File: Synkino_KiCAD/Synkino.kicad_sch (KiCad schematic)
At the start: 161 parts, among them J1 Pwr, J10 EYE8_OUT, J11 EYE4_OUT, J12 Eye, J13 EYE5_OUT, J2 Eye, J3 3.5mm, J4 Micro_SD_Card_Det_Hirose_DM3AT, J5 EYE1_OUT, J6 EYE6_OUT, J7 EYE2_OUT, J8 EYE7_OUT, J9 EYE3_OUT, Q1 IRF7319, Q2 BC847 o. SS8050, Q3 IRLML2244 o. AO3401A, SW1 Power, SW2 Rotary_Encoder_Switch, SW3 Reset, U1 ME6210A50PG, U10 ATMEGA328P-AU, U11 QRE1113GR, U12 QRE1113GR, U13 QRE1113GR, U14 QRE1113GR, U15 QRE1113GR, U16 QRE1113GR, U17 24LC256, U18 QRE1113GR, U2 ATMEGA328P-AU, U3 74HC4050, U4 SPIOLED128x64, U5 AP7312-1833W6-7, U6 74HC14, U7 VS1053B, U8 GS3005, U9 QRE1113GR, X1 FTDIconn, X2 ICSP, X3 FTDIconn, X4 ICSP, Y1 16Mhz, Y2 12.288MHz, Y3 16Mhz

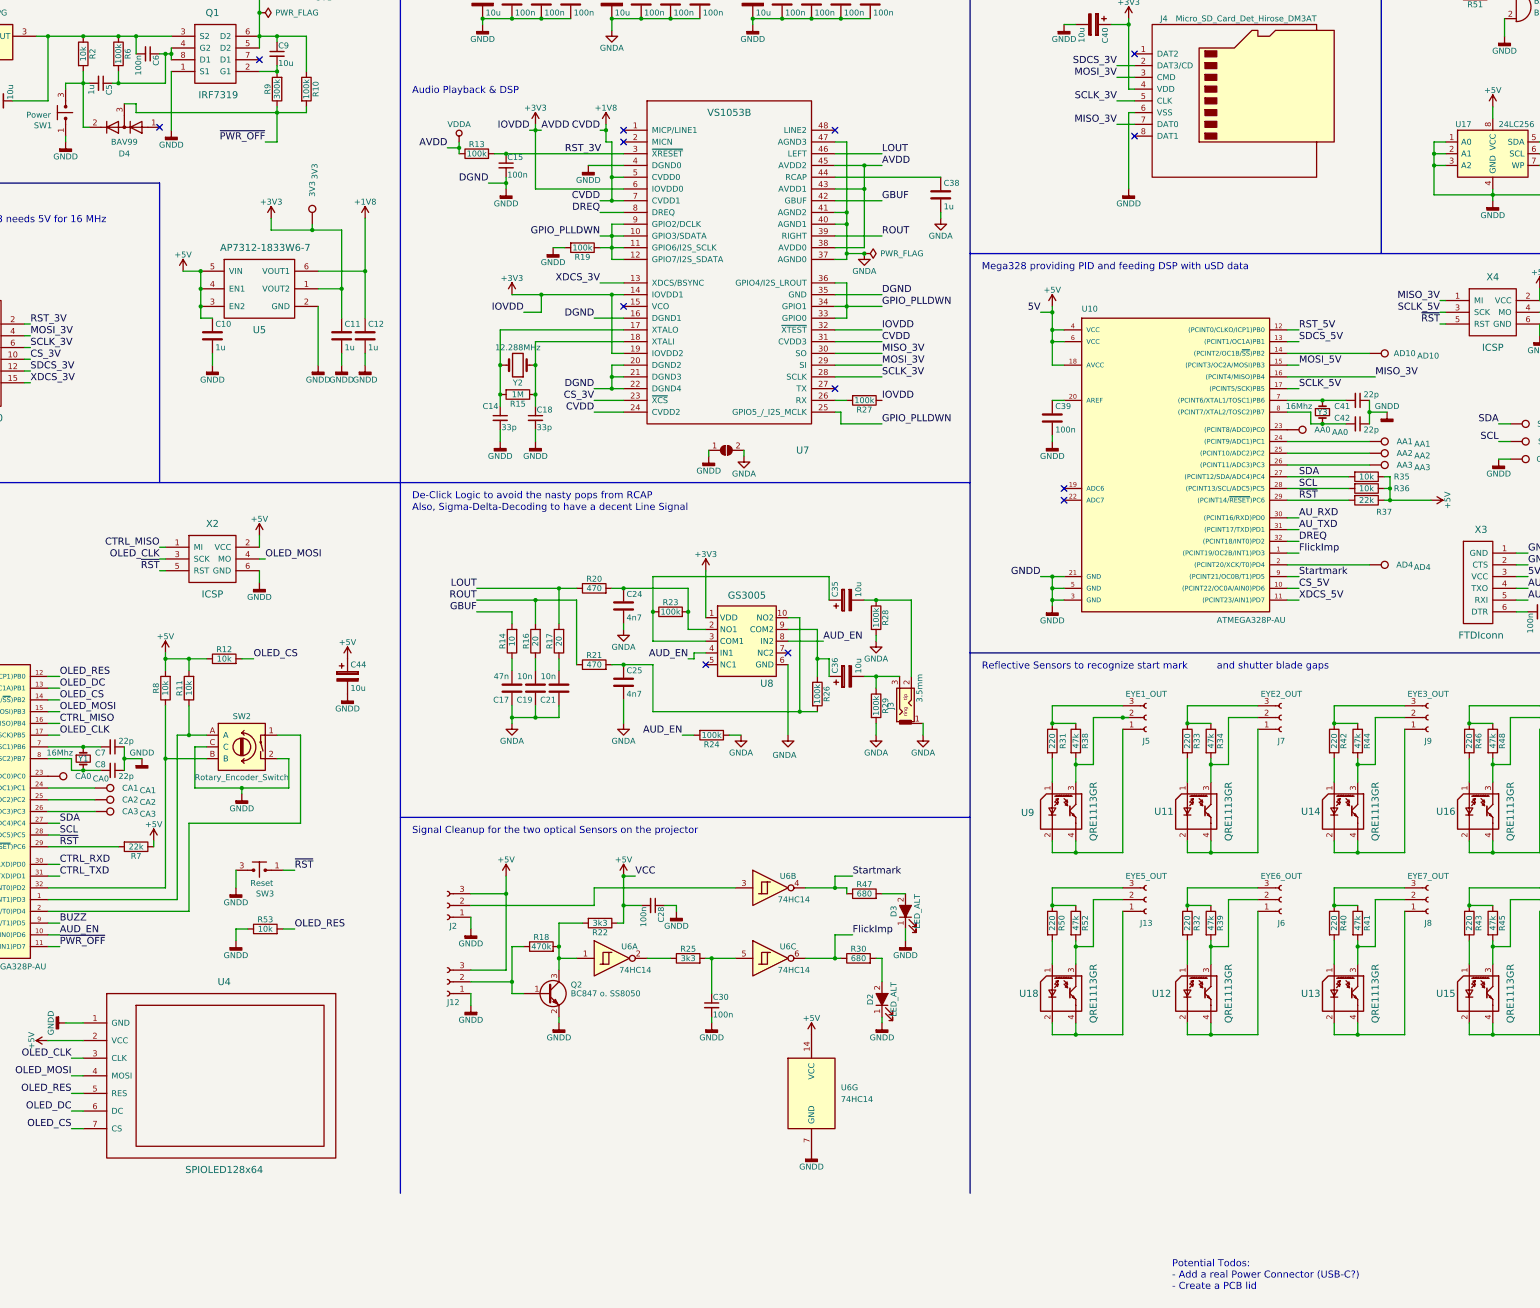
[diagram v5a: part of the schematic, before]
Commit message: Zero (legit) ERC errors
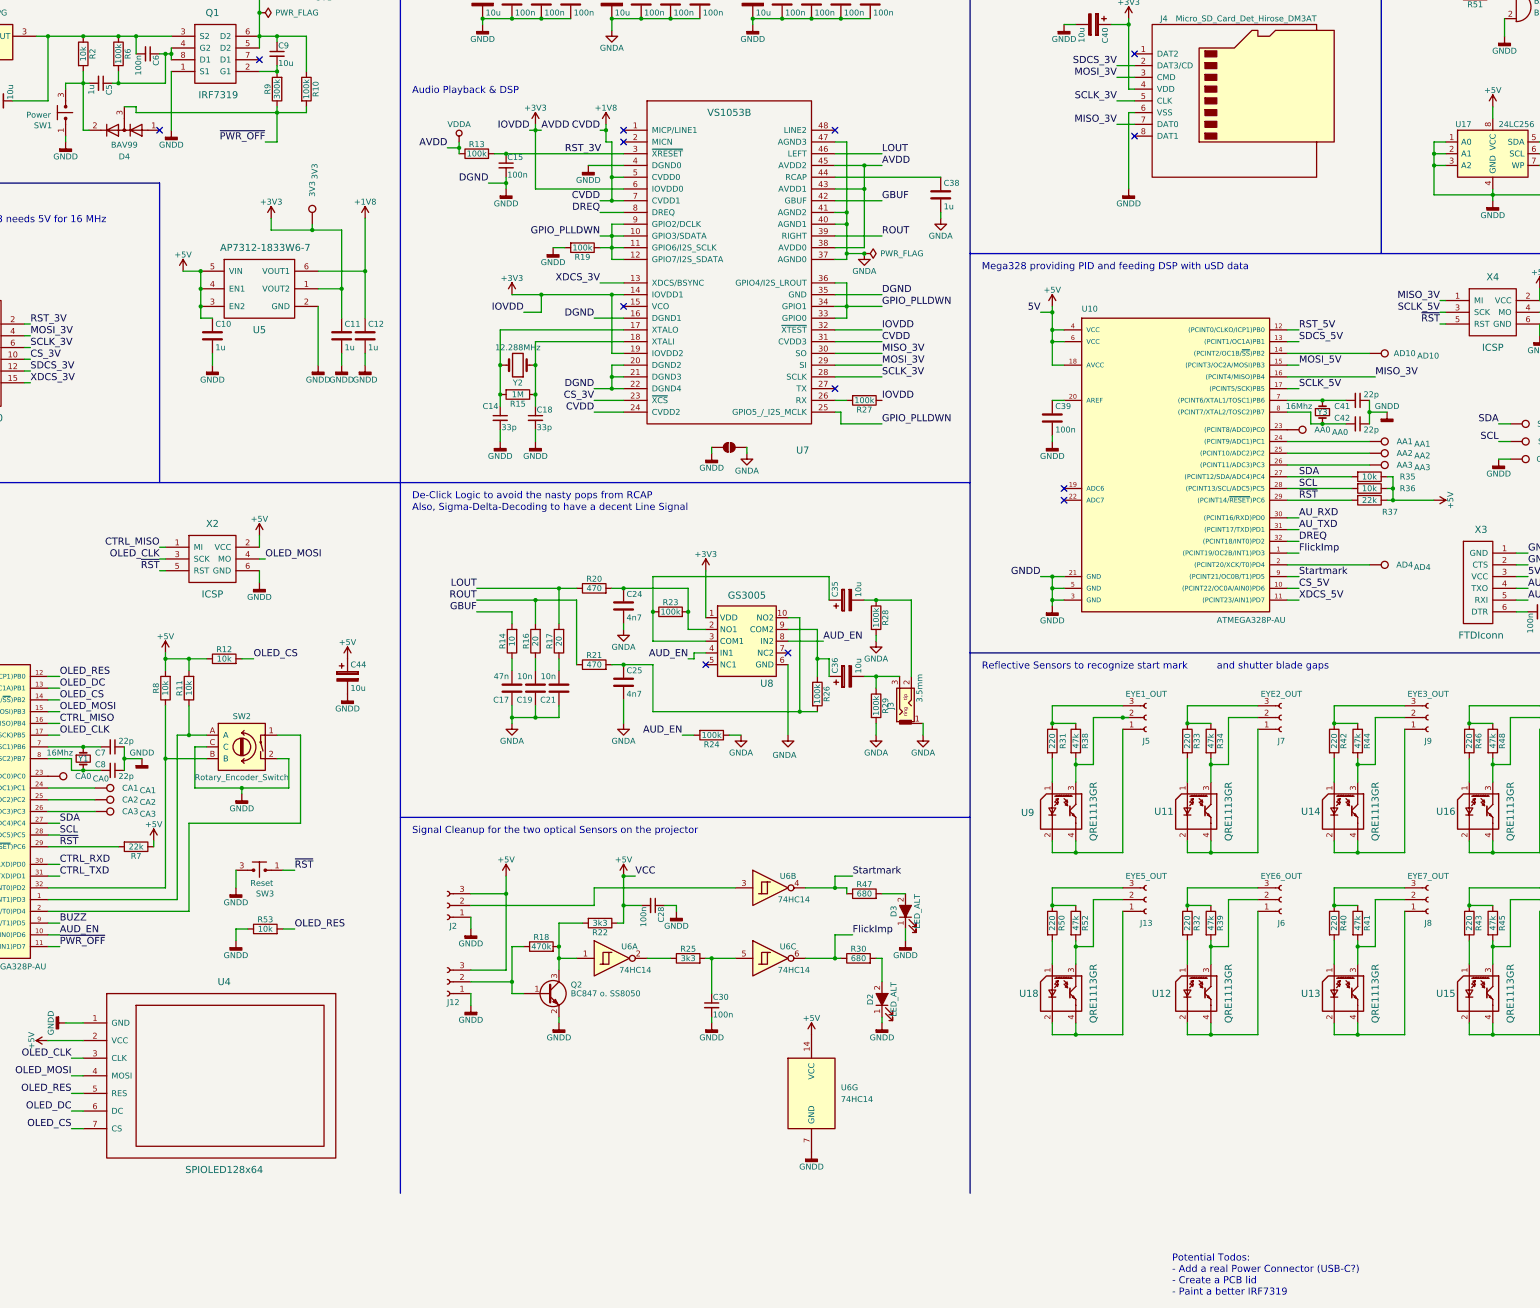
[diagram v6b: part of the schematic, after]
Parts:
- Q2: footprint Package_TO_SOT_SMD:SOT-23 -> TO_SOT_Packages_SMD:SOT-23
- Q3: footprint Package_TO_SOT_SMD:SOT-23 -> SOT-23
- U11, U12, U13, U14, U15, U16, U18, U9: footprint easyEDA:OPTO-SMD_QRE1113GR -> OptoDevice:OnSemi_CASE100CY
- U17: footprint Package_SO:SOIC-8_3.9x4.9mm_P1.27mm -> Housings_SOIC:SOIC-8_3.9x4.9mm_Pitch1.27mm
- U2: footprint Package_QFP:TQFP-32_7x7mm_P0.8mm -> Housings_QFP:TQFP-32_7x7mm_Pitch0.8mm
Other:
- note added: "Potential Todos: - Add a real Power Connector (USB-C?) - Create a PCB lid - Paint a better IRF7319"
- note removed: "Potential Todos: - Add a real Power Connector (USB-C?) - Create a PCB lid"
- moved on the sheet: D4, R35, R36, R37

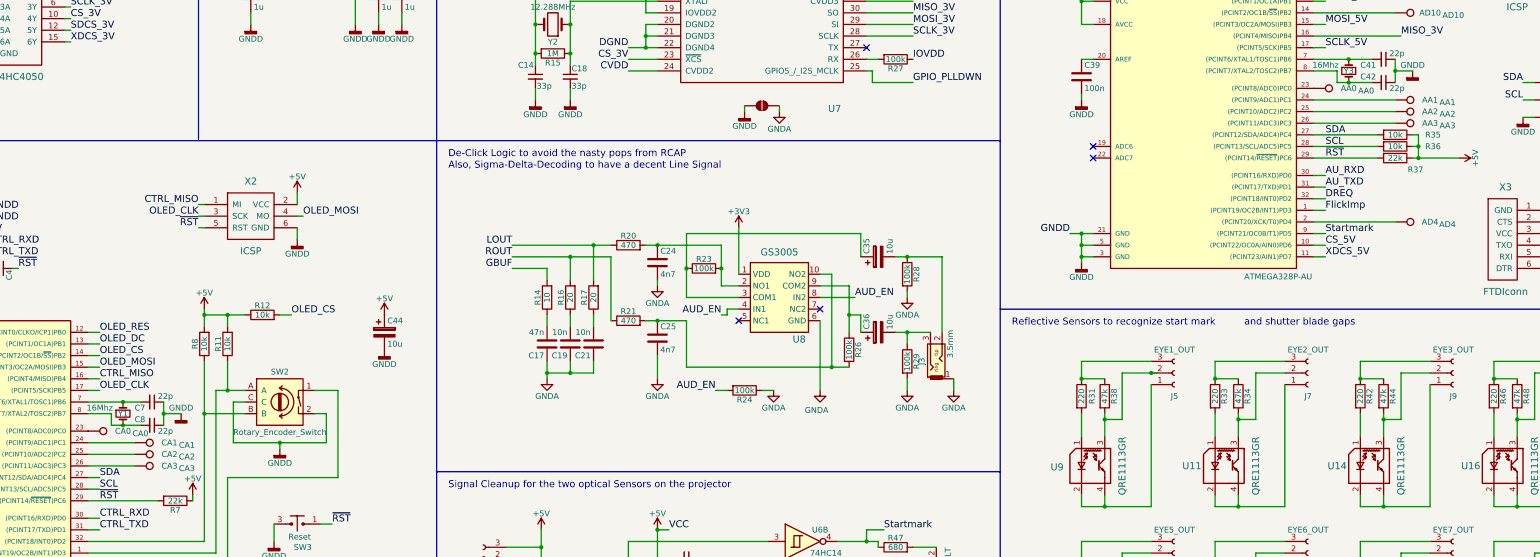
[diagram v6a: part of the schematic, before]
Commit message: Adding some TP labels
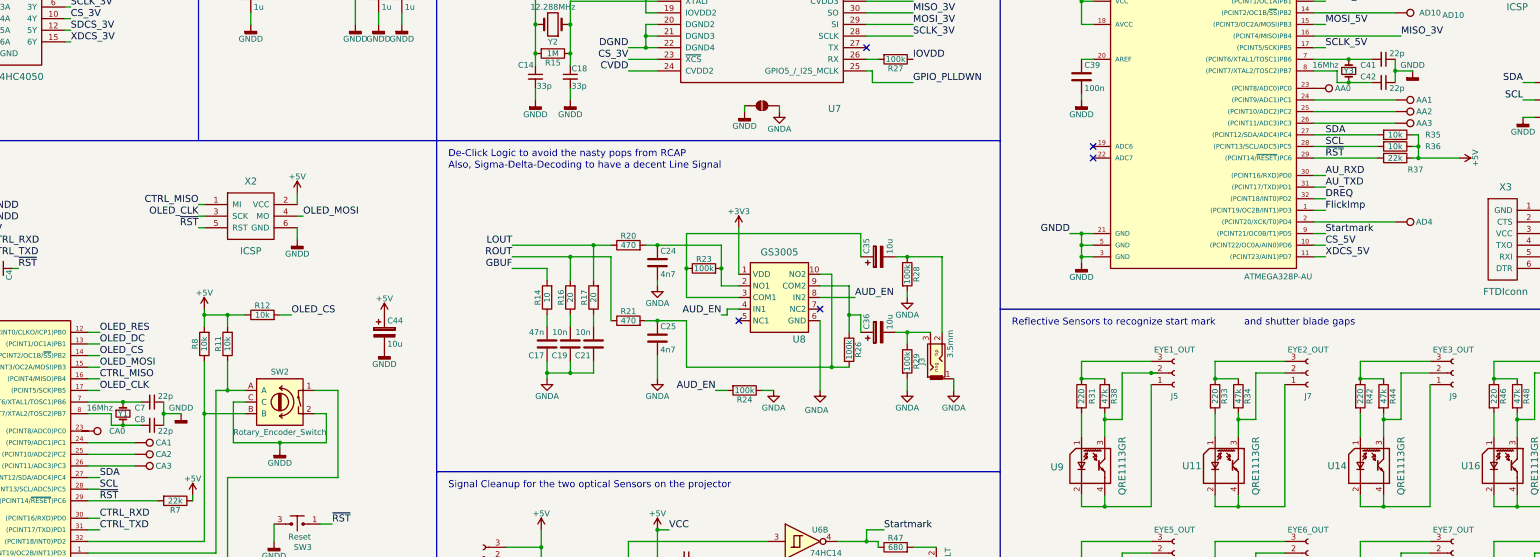
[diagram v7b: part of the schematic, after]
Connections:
- net at U2.23 ((PCINT8/ADC0)PC0): no longer CA0.1
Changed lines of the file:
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@@
 				)
 				(justify bottom)
+				(hide yes)
 			)
 		)
 		(property "Value" "AA3"
-			(at 365.76 127 90)
+			(at 364.49 127 90)
 			(effects
 				(font
@@
 				)
 				(justify bottom)
+				(hide yes)
 			)
 		)
 		(property "Value" "AA2"
-			(at 365.76 124.46 90)
+			(at 364.49 124.46 90)
 			(effects
 				(font
@@
 				)
 				(justify bottom)
+				(hide yes)
 			)
 		)
 		(property "Value" "AA1"
-			(at 365.76 121.92 90)
+			(at 364.49 121.92 90)
 			(effects
 				(font
@@
 				)
 				(justify bottom)
+				(hide yes)
 			)
 		)
 		(property "Value" "AA0"
-			(at 347.98 119.38 90)
+			(at 346.71 119.38 90)
 			(effects
 				(font
@@
 				)
 				(justify bottom)
+				(hide yes)
 			)
 		)
 		(property "Value" "AD4"
-			(at 365.76 148.59 90)
+			(at 364.49 148.59 90)
 			(effects
 				(font
@@
 				)
 				(justify bottom)
+				(hide yes)
 			)
 		)
 		(property "Value" "CA3"
-			(at 90.17 201.93 90)
+			(at 88.9 201.93 90)
 			(effects
 				(font
@@
 				)
 				(justify bottom)
+				(hide yes)
 			)
 		)
 		(property "Value" "CA2"
-			(at 90.17 199.39 90)
+			(at 88.9 199.39 90)
 			(effects
 				(font
@@
 				)
 				(justify bottom)
+				(hide yes)
 			)
 		)
 		(property "Value" "CA1"
-			(at 90.17 196.85 90)
+			(at 88.9 196.85 90)
 			(effects
 				(font
@@
 	(symbol
 		(lib_id "Connector:TestPoint")
-		(at 72.39 194.31 270)
+		(at 71.12 194.31 270)
 		(unit 1)
 		(exclude_from_sim no)
@@
 		(dnp no)
 		(property "Reference" "CA0"
-			(at 83.82 195.58 90)
+			(at 82.55 195.58 90)
 			(effects
 				(font
@@
 				)
 				(justify bottom)
+				(hide yes)
 			)
 		)
 		(property "Value" "CA0"
-			(at 80.01 194.31 90)
+			(at 78.74 194.31 90)
 			(effects
 				(font
@@
 		)
 		(property "Footprint" "TestPoint:TestPoint_THTPad_1.5x1.5mm_Drill0.7mm_no_name"
-			(at 72.39 199.39 0)
+			(at 71.12 199.39 0)
 			(effects
 				(font
@@
 		)
 		(property "Datasheet" "~"
-			(at 72.39 199.39 0)
+			(at 71.12 199.39 0)
 			(effects
 				(font
@@
 		)
 		(property "Description" "test point"
-			(at 72.39 194.31 0)
+			(at 71.12 194.31 0)
 			(effects
 				(font
@@
 		)
 		(property "Inventory" "-"
-			(at 72.39 194.31 0)
+			(at 71.12 194.31 0)
 			(effects
 				(font
@@
 		)
 		(property "LCSC" ""
-			(at 72.39 194.31 0)
-			(effects
-				(font
+			(at 71.12 194.31 0)
+			(effects
+				(font

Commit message: Pre Footprint-Fixing State
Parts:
- added GND2: GND, TestPoint:TestPoint_THTPad_1.5x1.5mm_Drill0.7mm_no_name, symbol Connector:TestPoint
- J3: footprint Peacemans_Footprints:SJ1-352XNG-3pin -> Peacemans Teile:SJ1-352XNG-3pin
- J4: footprint easyeda2kicad:SD-SMD_DM3AT-SF-PEJM5 -> easyEDA:SD-SMD_DM3AT-SF-PEJM5
- Q2: footprint TO_SOT_Packages_SMD:SOT-23 -> Package_TO_SOT_SMD:SOT-23
- Q3: footprint SOT-23 -> Package_TO_SOT_SMD:SOT-23
- SW2: footprint Peacemans_Footprints:SW_PEC11 -> Peacemans Teile:SW_PEC11
- U1: footprint easyeda2kicad:SOT-89-3_L4.5-W2.5-P1.50-LS4.2-BR -> Package_TO_SOT_SMD:SOT-89-3
- U10, U2: footprint Housings_QFP:TQFP-32_7x7mm_Pitch0.8mm -> Package_QFP:TQFP-32_7x7mm_P0.8mm
- U17: footprint Housings_SOIC:SOIC-8_3.9x4.9mm_Pitch1.27mm -> Package_SO:SOIC-8_3.9x4.9mm_P1.27mm
- U4: footprint Peacemans_Footprints:SPIOLED -> Peacemans Teile:SPIOLED_no_holes
- U5: footprint Peacemans_Footprints:AP7312 -> Peacemans Teile:AP7312
- U6: footprint (none) -> Package_SO:SOIC-14_3.9x8.7mm_P1.27mm
- U8: footprint Package_SO:MSOP-10_3x3mm_P0.5mm -> Package_SO:MSOP-10_3x3mm_P0.5mm_0.2_clearance
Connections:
- net GND: now also GND2.1
- net at U2.23 ((PCINT8/ADC0)PC0): now also CA0.1
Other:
- note removed: "10u"
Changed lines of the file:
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@@
 	(wire
 		(pts
+			(xy 386.08 130.81) (xy 388.62 130.81)
+		)
+		(stroke
+			(width 0)
+			(type default)
+		)
+	)
+	(wire
+		(pts
 			(xy 248.92 80.01) (xy 242.57 80.01)
 		)
@@
 	(text "6-18v\n"
 		(exclude_from_sim no)
-		(at 81.915 5.08 0)
+		(at 14.224 43.688 0)
 		(effects
 			(font
@@
 		)
 	)
-	(text "10u"
-		(exclude_from_sim no)
-		(at 82.55 8.255 0)
-		(effects
-			(font
-				(size 1.524 1.524)
-			)
-			(justify left bottom)
-		)
-	)
 	(text "and shutter blade gaps"
 		(exclude_from_sim no)
@@
 			)
 		)
-		(property "Footprint" "TO_SOT_Packages_SMD:SOT-23"
+		(property "Footprint" "Package_TO_SOT_SMD:SOT-23"
 			(at 185.42 243.205 0)
 			(effects
@@
 			)
 		)
-		(property "Footprint" "Peacemans_Footprints:AP7312"
+		(property "Footprint" "Peacemans Teile:AP7312"
 			(at 114.3 88.9 0)
 			(effects
@@
 			)
 		)
-		(property "Footprint" "Package_SO:MSOP-10_3x3mm_P0.5mm"
+		(property "Footprint" "Package_SO:MSOP-10_3x3mm_P0.5mm_0.2_clearance"
 			(at 223.52 177.8 0)
 			(effects
@@
 			)
 		)
-		(property "Footprint" "easyeda2kicad:SD-SMD_DM3AT-SF-PEJM5"
+		(property "Footprint" "easyEDA:SD-SMD_DM3AT-SF-PEJM5"
 			(at 382.27 30.48 0)
 			(effects
@@
 			)
 		)
-		(property "Footprint" "Housings_QFP:TQFP-32_7x7mm_Pitch0.8mm"
+		(property "Footprint" "Package_QFP:TQFP-32_7x7mm_P0.8mm"
 			(at 314.96 125.73 0)
 			(effects
@@
 			)
 		)
-		(property "Footprint" "Peacemans_Footprints:SPIOLED"
+		(property "Footprint" "Peacemans Teile:SPIOLED_no_holes"
 			(at 118.11 276.86 0)
 			(effects
@@
 			)
 		)
-		(property "Footprint" "Housings_QFP:TQFP-32_7x7mm_Pitch0.8mm"
+		(property "Footprint" "Package_QFP:TQFP-32_7x7mm_P0.8mm"
 			(at 46.99 200.66 0)
 			(effects
@@
 			)
 		)
-		(property "Footprint" "Peacemans_Footprints:SW_PEC11"
+		(property "Footprint" "Peacemans Teile:SW_PEC11"
 			(at 111.76 183.896 0)
 			(effects
@@
 	(symbol
 		(lib_id "Connector:TestPoint")
-		(at 71.12 194.31 270)
+		(at 72.39 194.31 270)
 		(unit 1)
 		(exclude_from_sim no)
@@
 		(dnp no)
 		(property "Reference" "CA0"
-			(at 82.55 195.58 90)
+			(at 83.82 195.58 90)
 			(effects
 				(font
@@
 		)
 		(property "Value" "CA0"
-			(at 78.74 194.31 90)
+			(at 78.486 195.072 90)
 			(effects
 				(font
@@
 		)
 		(property "Footprint" "TestPoint:TestPoint_THTPad_1.5x1.5mm_Drill0.7mm_no_name"
-			(at 71.12 199.39 0)
+			(at 72.39 199.39 0)
 			(effects
 				(font
@@
 		)
 		(property "Datasheet" "~"
-			(at 71.12 199.39 0)
+			(at 72.39 199.39 0)
 			(effects
 				(font
@@
 		)
 		(property "Description" "test point"
-			(at 71.12 194.31 0)
+			(at 72.39 194.31 0)
 			(effects
 				(font
@@
 		)
 		(property "Inventory" "-"
-			(at 71.12 194.31 0)
+			(at 72.39 194.31 0)
 			(effects
 				(font
@@
 		)
 		(property "LCSC" ""
-			(at 71.12 194.31 0)
+			(at 72.39 194.31 0)
 			(effects
 				(font
@@
 			)
 		)
-		(property "Footprint" "Peacemans_Footprints:SJ1-352XNG-3pin"
+		(property "Footprint" "Peacemans Teile:SJ1-352XNG-3pin"
 			(at 256.54 171.45 0)
 			(effects
@@
 			)
 		)
-		(property "Footprint" "SOT-23"
+		(property "Footprint" "Package_TO_SOT_SMD:SOT-23"
 			(at 34.29 32.639 0)
 			(effects
@@
 			)
 		)
-		(property "Footprint" "Housings_SOIC:SOIC-8_3.9x4.9mm_Pitch1.27mm"
+		(property "Footprint" "Package_SO:SOIC-8_3.9x4.9mm_P1.27mm"
 			(at 386.08 66.04 0)
 			(effects
@@
 	)
 	(symbol
+		(lib_id "Connector:TestPoint")
+		(at 388.62 130.81 270)
+		(unit 1)
+		(exclude_from_sim no)
+		(in_bom yes)
+		(on_board yes)
+		(dnp no)
+		(property "Reference" "GND2"
+			(at 400.05 132.08 90)
+			(effects
+				(font
+					(size 1.27 1.27)
+				)
+				(justify bottom)
+				(hide yes)
+			)
+		)
+		(property "Value" "GND"
+			(at 396.24 130.81 90)
+			(effects
+				(font
+					(size 1.27 1.27)
+				)
+			)
+		)
+		(property "Footprint" "TestPoint:TestPoint_THTPad_1.5x1.5mm_Drill0.7mm_no_name"
+			(at 388.62 135.89 0)
+			(effects
+				(font
+					(size 1.27 1.27)
+				)
+				(hide yes)
+			)
+		)
+		(property "Datasheet" "~"
+			(at 388.62 135.89 0)
+			(effects
+				(font
+					(size 1.27 1.27)
+				)
+				(hide yes)
+			)
+		)
+		(property "Description" "test point"
+			(at 388.62 130.81 0)
+			(effects
+				(font
+					(size 1.27 1.27)
+				)
+				(hide yes)
+			)
+		)
+		(property "Inventory" "-"
+			(at 388.62 130.81 0)
+			(effects
+				(font
+					(size 1.27 1.27)
+				)
+				(hide yes)
+			)
+		)
+		(property "LCSC" ""
+			(at 388.62 130.81 0)
+			(effects
+				(font
+					(size 1.27 1.27)
+				)
+				(hide yes)
+			)
+		)
+		(pin "1"
+		)
+		(instances
+			(project "Synkino"
+				(path "/9d4924d9-a2ad-42f2-a951-8d7a9cc74761"
+					(reference "GND2")
+					(unit 1)
+				)
+			)
+		)
+	)
+	(symbol
 		(lib_id "easyEDA:ME6210A50PG")
 		(at 57.15 39.37 0)
@@
 			)
 		)
-		(property "Footprint" "easyeda2kicad:SOT-89-3_L4.5-W2.5-P1.50-LS4.2-BR"
+		(property "Footprint" "Package_TO_SOT_SMD:SOT-89-3"
 			(at 57.15 52.07 0)
 			(effects
@@
 			)
 		)
-		(property "Footprint" ""
+		(property "Footprint" "Package_SO:SOIC-14_3.9x8.7mm_P1.27mm"
 			(at 237.49 262.89 0)
 			(effects
@@
 					(unit 1)
 				)
+			)
+		)
+	)
+	(symbol
+		(lib_id "power:GNDD")
+		(at 386.08 130.81 0)
+		(unit 1)
+		(exclude_from_sim no)
+		(in_bom yes)
+		(on_board yes)
+		(dnp no)
+		(property "Reference" "#PWR082"
+			(at 386.08 137.16 0)
+			(effects
+				(font
+					(size 1.27 1.27)
+				)
+				(hide yes)
+			)
+		)
+		(property "Value" "GNDD"
+			(at 386.08 133.985 0)
+			(effects
+				(font
+					(size 1.27 1.27)
+				)
+			)
+		)
+		(property "Footprint" ""
+			(at 386.08 130.81 0)
+			(effects
+				(font
+					(size 1.27 1.27)
+				)
+				(hide yes)
+			)
+		)
+		(property "Datasheet" ""
+			(at 386.08 130.81 0)
+			(effects
+				(font
+					(size 1.27 1.27)
+				)
+				(hide yes)
+			)
+		)
+		(property "Description" "Power symbol creates a global label with name \"GNDD\" , digital ground"
+			(at 386.08 130.81 0)
+			(effects
+				(font
+					(size 1.27 1.27)
+				)
+				(hide yes)
+			)
+		)
+		(pin "1"
+		)
+		(instances
+			(project "Synkino"
+				(path "/9d4924d9-a2ad-42f2-a951-8d7a9cc74761"
+					(reference "#PWR082")
+					(unit 1)
+				)
